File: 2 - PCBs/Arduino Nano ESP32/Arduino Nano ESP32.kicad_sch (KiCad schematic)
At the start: 36 parts, among them J1 USB4056-03-A, M1 NORA-W106-10B, U2 MP9943GQ-Z, U3 GD25B128EWIGR, Y1 CM315D32768DZFT

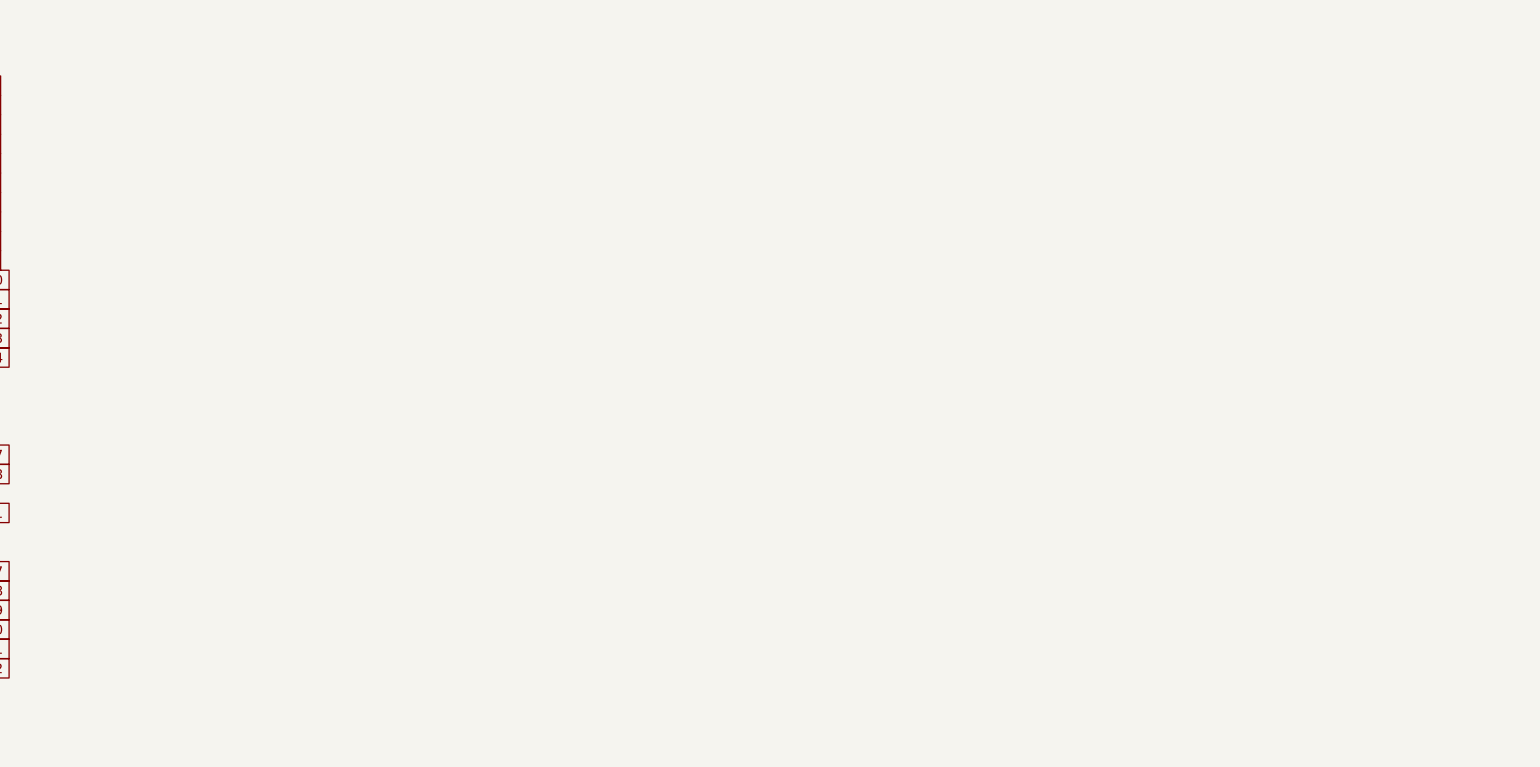
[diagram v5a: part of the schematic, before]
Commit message: Finished headers schematic
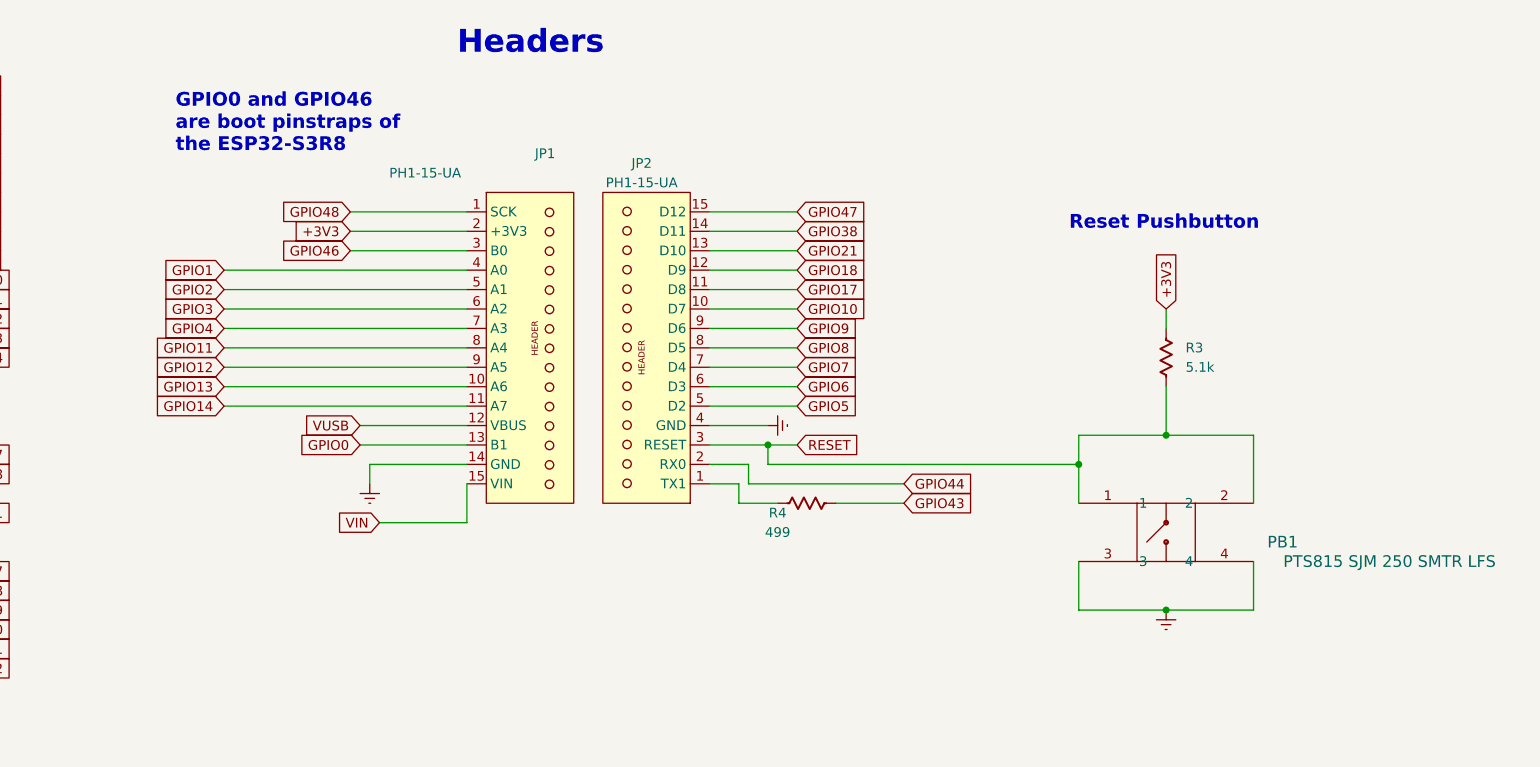
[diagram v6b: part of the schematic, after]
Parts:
- added JP1, JP2: PH1-15-UA, symbol PH1-15-UA:PH1-15-UA
- added PB1: PTS815 SJM 250 SMTR LFS, PTS815_SJM_250_SMTR_LFS: PTS815_SJM_250_SMTR_LFS, symbol PTS815_SJM_250_SMTR_LFS:PTS815_SJM_250_SMTR_LFS
- added R3: 5.1k, Resistor_SMD_AKL:R_0603_1608Metric, symbol Resistor_US_AKL:R_0603
- added R4: 499, Resistor_SMD_AKL:R_0603_1608Metric, symbol Resistor_US_AKL:R_0603
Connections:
- net +3V3: now also JP1.2 (+3V3), R3.1
- net Earth: now also JP1.14 (GND), JP2.4 (GND), PB1.3, PB1.4
- net GPIO0: now also JP1.13 (B1)
- net GPIO1: now also JP1.4 (A0)
- net GPIO10: now also JP2.10 (D7)
- net GPIO11: now also JP1.8 (A4)
- net GPIO12: now also JP1.9 (A5)
- net GPIO13: now also JP1.10 (A6)
- net GPIO14: now also JP1.11 (A7)
- net GPIO17: now also JP2.11 (D8)
- net GPIO18: now also JP2.12 (D9)
- net GPIO2: now also JP1.5 (A1)
- net GPIO21: now also JP2.13 (D10)
- net GPIO3: now also JP1.6 (A2)
- net GPIO38: now also JP2.14 (D11)
- net GPIO4: now also JP1.7 (A3)
- net GPIO43: now also R4.2
- net GPIO44: now also JP2.2 (RX0)
- net GPIO46: now also JP1.3 (B0)
- net GPIO47: now also JP2.15 (D12)
- net GPIO48: now also JP1.1 (SCK)
- net GPIO5: now also JP2.5 (D2)
- net GPIO6: now also JP2.6 (D3)
- net GPIO7: now also JP2.7 (D4)
- net GPIO8: now also JP2.8 (D5)
- net GPIO9: now also JP2.9 (D6)
- net RESET: now also JP2.3 (RESET), PB1.1, PB1.2, R3.2
- net VIN: now also JP1.15 (VIN)
- net VUSB: now also JP1.12 (VBUS)
- new net: JP2.1 (TX1), R4.1
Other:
- note added: "GPIO0 and GPIO46 are boot pinstraps of the ESP32-S3R8"
- note added: "Headers"
- note added: "Reset Pushbutton"

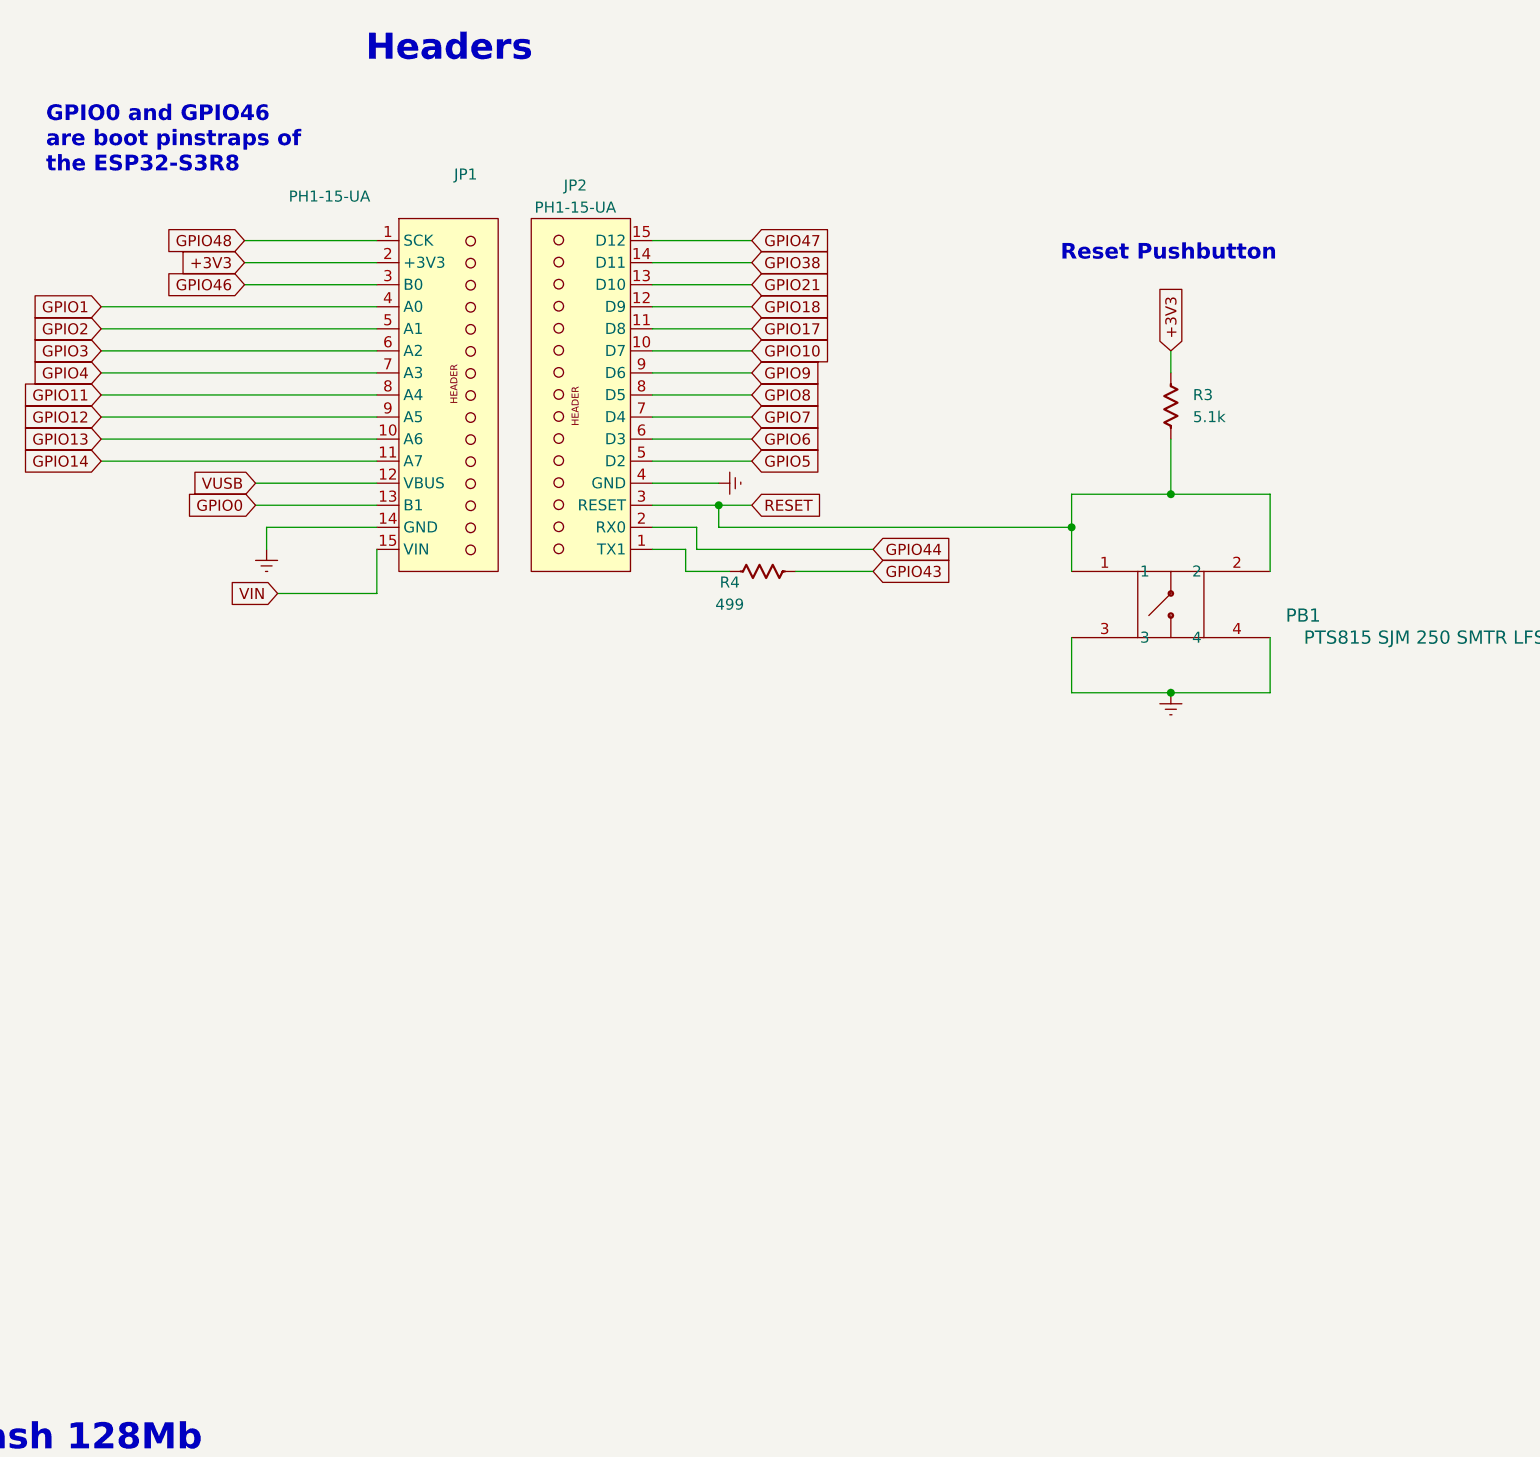
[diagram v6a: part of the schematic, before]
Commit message: Finished LED Schematics
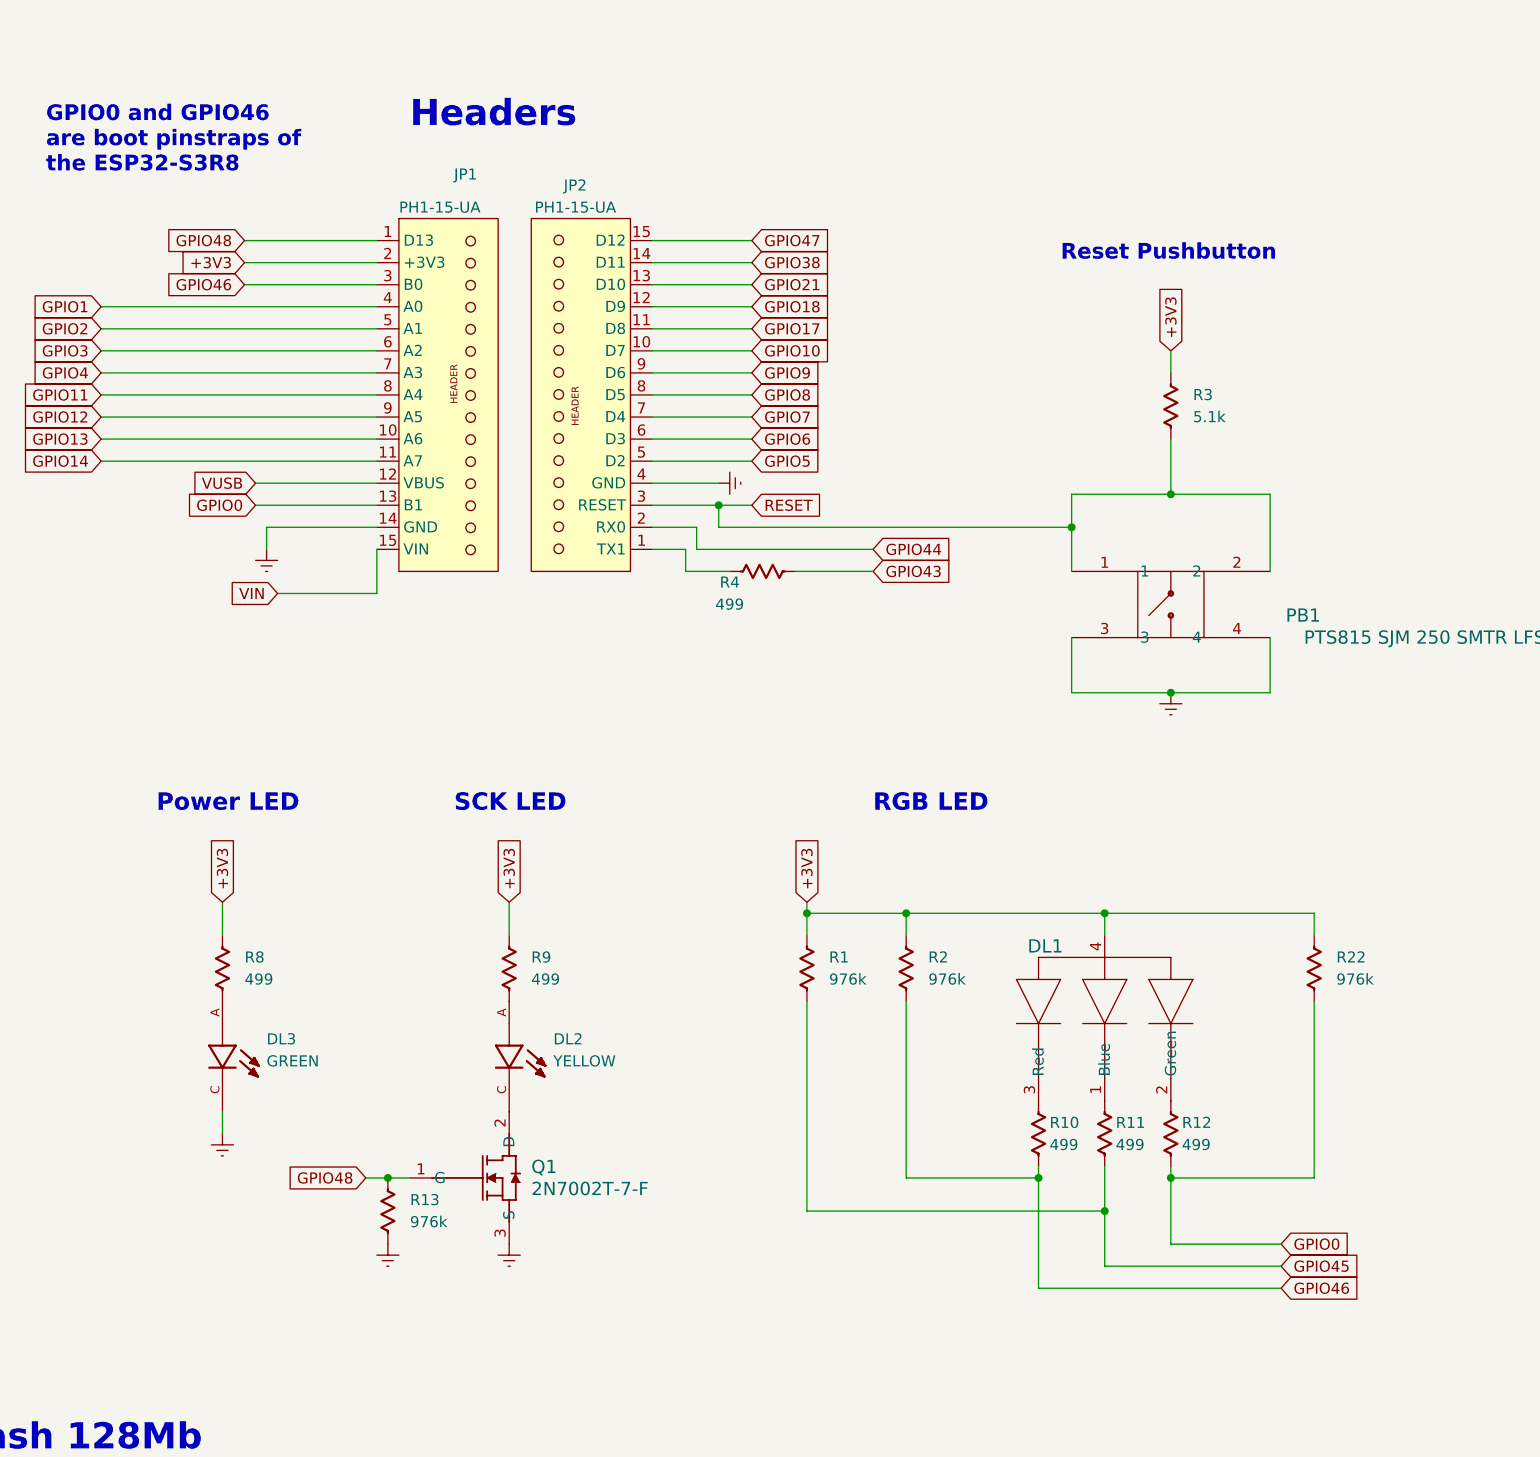
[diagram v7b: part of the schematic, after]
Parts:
- added DL1: ~, 0404_RGB_LED:0404_RGB_LED, symbol 0404_RGB_LED:0404_RGB_LED
- added DL2: YELLOW, 0603_LED:0603_LED, symbol 0603_LED:0603_LED
- added DL3: GREEN, 0603_LED:0603_LED, symbol 0603_LED:0603_LED
- added Q1: 2N7002T-7-F, 2N7002T-7-F:2N7002T-7-F, symbol 2N7002T-7-F:2N7002T-7-F
- added R1, R13, R2, R22: 976k, Resistor_SMD_AKL:R_0603_1608Metric, symbol Resistor_US_AKL:R_0603
- added R10, R11, R12, R8, R9: 499, Resistor_SMD_AKL:R_0603_1608Metric, symbol Resistor_US_AKL:R_0603
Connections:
- net +3V3: now also DL1.4, R1.1, R2.1, R22.1, R8.1, R9.1
- net Earth: now also DL3.C, Q1.3 (S), R13.2
- net GPIO0: now also R12.2, R22.2
- net GPIO45: now also R1.2, R11.2
- net GPIO46: now also R10.2, R2.2
- net GPIO48: now also Q1.1 (G), R13.1
- new net: DL2.C, Q1.2 (D)
- new net: DL1.1 (Blue), R11.1
- new net: DL1.3 (Red), R10.1
- new net: DL2.A, R9.2
- new net: DL3.A, R8.2
- new net: DL1.2 (Green), R12.1
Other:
- note added: "Power LED"
- note added: "RGB LED"
- note added: "SCK LED"
